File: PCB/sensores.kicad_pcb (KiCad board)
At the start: 2 copper layers, 80.6 x 50 mm, 7 parts, among them P10 CONN_01X07, P11 CONN_01X07, P15 DHT22, P16 GY-87, P2 CONN_01X04, P3 CONN_01X04

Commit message: Add logo ElectronicCats
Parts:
- added G***: LOGO, theinventorhouse:electronic_cats_logo_8x6, F.Cu at (95.5, 94.7)

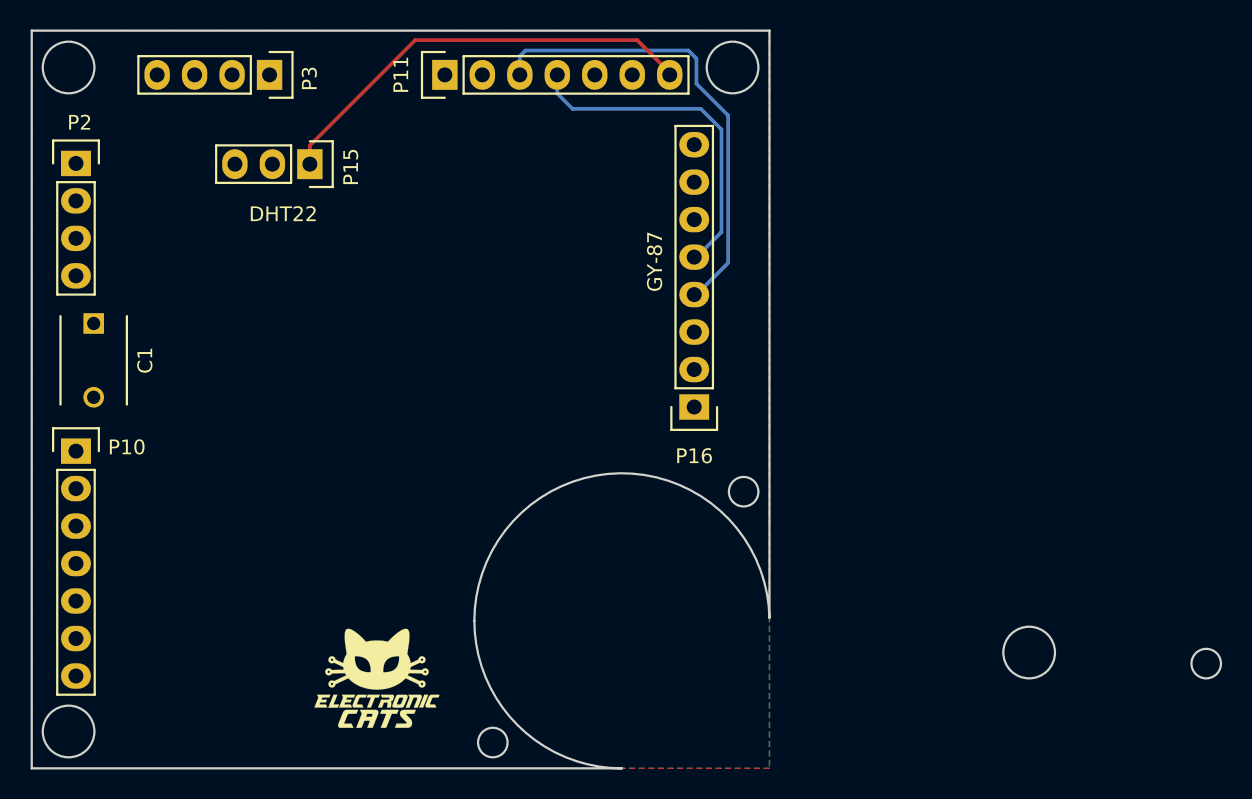
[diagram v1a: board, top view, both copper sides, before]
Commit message: Fix bug GND of GY-87
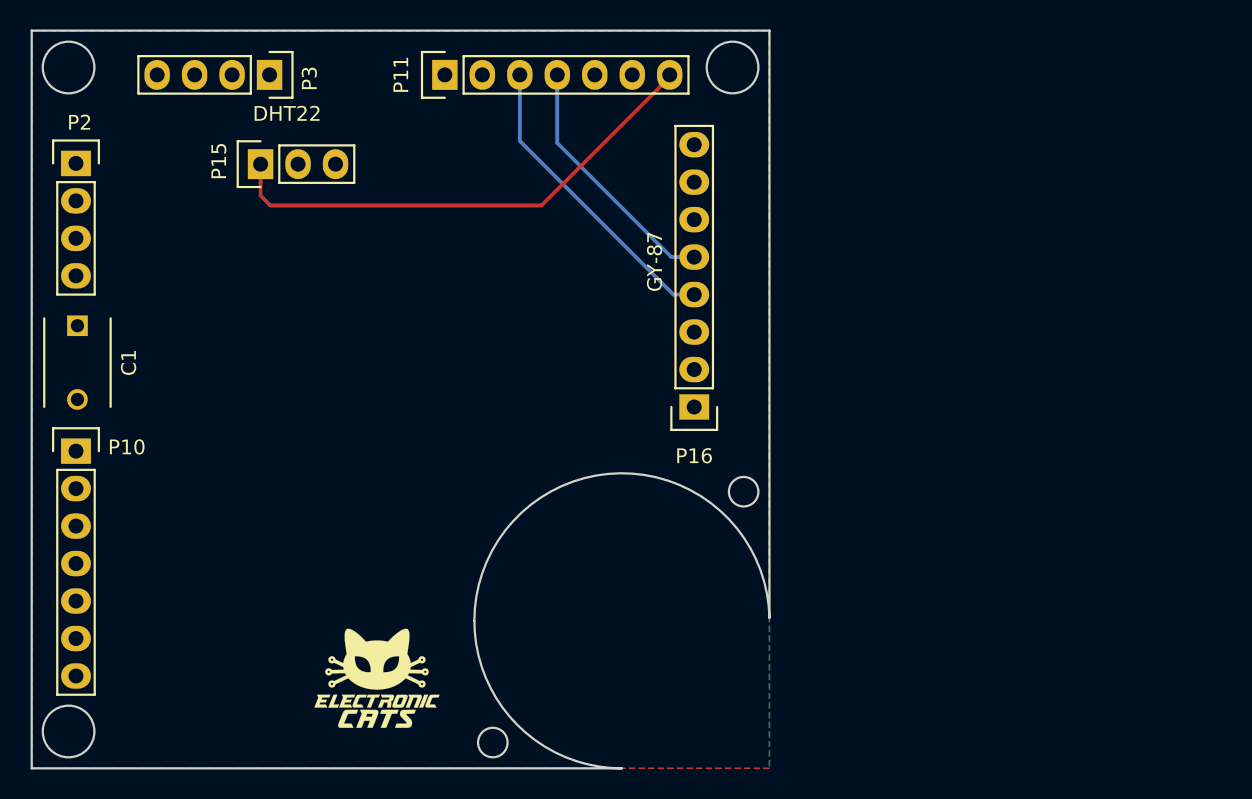
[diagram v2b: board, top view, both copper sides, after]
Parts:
- moved P15 3.34 mm to (87.7, 59.8), turned to 90 degrees
- moved C1 1.11 mm to (75.2, 70.8)
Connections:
- P16 pad 2: GND -> Net-(P16-Pad2)
- P16 pad 3: Net-(P16-Pad3) -> GND
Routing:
- net SCL: track 31.5 -> 20.8 mm
- net SDA: track 22.9 -> 18.5 mm
- net DHT/D6: track 29.7 -> 34.1 mm
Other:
- board size 80.6 x 50 mm -> 50 x 50 mm

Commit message: PCB final
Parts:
- moved P15 1.20 mm to (86.5, 59.8)
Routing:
- net +BATT: track 0.00 -> 78.5 mm
- added copper zone on B.Cu, net GND
- removed copper zone on B.Cu, net +BATT
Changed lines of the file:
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@@
 (kicad_pcb (version 4) (host pcbnew 4.0.0-rc1-stable)
   (general
-    (links 102)
-    (no_connects 72)
-    (area 72.074999 50.674999 122.225001 100.825001)
+    (links 11)
+    (no_connects 4)
+    (area 48.501725 43.9 139.328572 109.450001)
     (thickness 1.6)
     (drawings 22)
-    (tracks 17)
+    (tracks 32)
     (zones 0)
     (modules 8)
@@
     (add_net MOSI)
     (add_net NSS)
-    (add_net "Net-(A1-Pad1)")
-    (add_net "Net-(D1-Pad2)")
-    (add_net "Net-(MODULE1-Pad10)")
-    (add_net "Net-(MODULE1-Pad11)")
-    (add_net "Net-(MODULE1-Pad5)")
-    (add_net "Net-(MODULE1-Pad6)")
-    (add_net "Net-(MODULE1-Pad7)")
-    (add_net "Net-(MODULE1-Pad8)")
     (add_net "Net-(P16-Pad2)")
-    (add_net "Net-(P5-Pad2)")
-    (add_net "Net-(RAW1-Pad1)")
-    (add_net "Net-(RAW1-Pad19)")
-    (add_net "Net-(RAW1-Pad2)")
-    (add_net "Net-(RAW1-Pad21)")
-    (add_net "Net-(RAW1-Pad3)")
-    (add_net "Net-(RAW1-Pad4)")
-    (add_net "Net-(RAW1-Pad5)")
-    (add_net "Net-(RAW1-Pad6)")
-    (add_net "Net-(RAW1-Pad7)")
-    (add_net "Net-(RAW1-Pad8)")
-    (add_net "Net-(RAW1-Pad9)")
-    (add_net "Net-(U1-Pad1)")
-    (add_net "Net-(U1-Pad2)")
-    (add_net "Net-(U2-Pad11)")
-    (add_net "Net-(U2-Pad12)")
-    (add_net "Net-(U2-Pad15)")
-    (add_net "Net-(U2-Pad16)")
-    (add_net "Net-(U2-Pad7)")
     (add_net RST)
     (add_net SCK)
@@
     (add_net S_RX)
     (add_net S_TX)
+  )
+  (module Pin_Headers:Pin_Header_Straight_1x03 (layer F.Cu)
+    (at 86.46 59.8 90)
+    (descr "Through hole pin header")
+    (tags "pin header")
+    (fp_text reference P15 (at 0.2 -2.8 90) (layer F.SilkS)
+      (effects (font (size 1 1) (thickness 0.15)))
+    )
+    (fp_text value DHT22 (at 3.4 1.8 180) (layer F.SilkS)
+      (effects (font (size 1 1) (thickness 0.15)))
+    )
+    (fp_line (start -1.75 -1.75) (end -1.75 6.85) (layer F.CrtYd) (width 0.05))
+    (fp_line (start 1.75 -1.75) (end 1.75 6.85) (layer F.CrtYd) (width 0.05))
+    (fp_line (start -1.75 -1.75) (end 1.75 -1.75) (layer F.CrtYd) (width 0.05))
+    (fp_line (start -1.75 6.85) (end 1.75 6.85) (layer F.CrtYd) (width 0.05))
+    (fp_line (start -1.27 1.27) (end -1.27 6.35) (layer F.SilkS) (width 0.15))
+    (fp_line (start -1.27 6.35) (end 1.27 6.35) (layer F.SilkS) (width 0.15))
+    (fp_line (start 1.27 6.35) (end 1.27 1.27) (layer F.SilkS) (width 0.15))
+    (fp_line (start 1.55 -1.55) (end 1.55 0) (layer F.SilkS) (width 0.15))
+    (fp_line (start 1.27 1.27) (end -1.27 1.27) (layer F.SilkS) (width 0.15))
+    (fp_line (start -1.55 0) (end -1.55 -1.55) (layer F.SilkS) (width 0.15))
+    (fp_line (start -1.55 -1.55) (end 1.55 -1.55) (layer F.SilkS) (width 0.15))
+    (pad 1 thru_hole rect (at 0 0 90) (size 2.032 1.7272) (drill 1.016) (layers *.Cu *.Mask F.SilkS)
+      (net 7 DHT/D6))
+    (pad 2 thru_hole oval (at 0 2.54 90) (size 2.032 1.7272) (drill 1.016) (layers *.Cu *.Mask F.SilkS)
+      (net 2 +BATT))
+    (pad 3 thru_hole oval (at 0 5.08 90) (size 2.032 1.7272) (drill 1.016) (layers *.Cu *.Mask F.SilkS)
+      (net 1 GND))
+    (model Pin_Headers.3dshapes/Pin_Header_Straight_1x03.wrl
+      (at (xyz 0 -0.1 0))
+      (scale (xyz 1 1 1))
+      (rotate (xyz 0 0 90))
+    )
   )
   (module Pin_Headers:Pin_Header_Straight_1x08 (layer F.Cu)
@@
     (model Pin_Headers.3dshapes/Pin_Header_Straight_1x07.wrl
       (at (xyz 0 -0.3 0))
-      (scale (xyz 1 1 1))
-      (rotate (xyz 0 0 90))
-    )
-  )
-  (module Pin_Headers:Pin_Header_Straight_1x03 (layer F.Cu)
-    (at 87.66 59.8 90)
-    (descr "Through hole pin header")
-    (tags "pin header")
-    (fp_text reference P15 (at 0.2 -2.8 90) (layer F.SilkS)
-      (effects (font (size 1 1) (thickness 0.15)))
-    )
-    (fp_text value DHT22 (at 3.4 1.8 180) (layer F.SilkS)
-      (effects (font (size 1 1) (thickness 0.15)))
-    )
-    (fp_line (start -1.75 -1.75) (end -1.75 6.85) (layer F.CrtYd) (width 0.05))
-    (fp_line (start 1.75 -1.75) (end 1.75 6.85) (layer F.CrtYd) (width 0.05))
-    (fp_line (start -1.75 -1.75) (end 1.75 -1.75) (layer F.CrtYd) (width 0.05))
-    (fp_line (start -1.75 6.85) (end 1.75 6.85) (layer F.CrtYd) (width 0.05))
-    (fp_line (start -1.27 1.27) (end -1.27 6.35) (layer F.SilkS) (width 0.15))
-    (fp_line (start -1.27 6.35) (end 1.27 6.35) (layer F.SilkS) (width 0.15))
-    (fp_line (start 1.27 6.35) (end 1.27 1.27) (layer F.SilkS) (width 0.15))
-    (fp_line (start 1.55 -1.55) (end 1.55 0) (layer F.SilkS) (width 0.15))
-    (fp_line (start 1.27 1.27) (end -1.27 1.27) (layer F.SilkS) (width 0.15))
-    (fp_line (start -1.55 0) (end -1.55 -1.55) (layer F.SilkS) (width 0.15))
-    (fp_line (start -1.55 -1.55) (end 1.55 -1.55) (layer F.SilkS) (width 0.15))
-    (pad 1 thru_hole rect (at 0 0 90) (size 2.032 1.7272) (drill 1.016) (layers *.Cu *.Mask F.SilkS)
-      (net 7 DHT/D6))
-    (pad 2 thru_hole oval (at 0 2.54 90) (size 2.032 1.7272) (drill 1.016) (layers *.Cu *.Mask F.SilkS)
-      (net 2 +BATT))
-    (pad 3 thru_hole oval (at 0 5.08 90) (size 2.032 1.7272) (drill 1.016) (layers *.Cu *.Mask F.SilkS)
-      (net 1 GND))
-    (model Pin_Headers.3dshapes/Pin_Header_Straight_1x03.wrl
-      (at (xyz 0 -0.1 0))
       (scale (xyz 1 1 1))
       (rotate (xyz 0 0 90))
@@
   (gr_line (start 72.15 100.75) (end 72.15 50.75) (layer Edge.Cuts) (width 0.15))
   (gr_line (start 72.15 50.75) (end 122.15 50.75) (layer Edge.Cuts) (width 0.15))
+  (segment (start 89 59.8) (end 89 61.066) (width 0.25) (layer B.Cu) (net 2))
+  (segment (start 89 61.066) (end 90.2 62.266) (width 0.25) (layer B.Cu) (net 2))
+  (segment (start 90.2 62.266) (end 90.2 65.8) (width 0.25) (layer B.Cu) (net 2))
+  (segment (start 75.15 79.25) (end 76.75 79.25) (width 0.25) (layer B.Cu) (net 2) (status 400000))
+  (segment (start 77.4 72.9) (end 75.25 70.75) (width 0.25) (layer B.Cu) (net 2) (status 800000))
+  (segment (start 77.4 78.6) (end 77.4 72.9) (width 0.25) (layer B.Cu) (net 2))
+  (segment (start 76.75 79.25) (end 77.4 78.6) (width 0.25) (layer B.Cu) (net 2))
+  (segment (start 101.8 65.8) (end 102.69 65.8) (width 0.25) (layer B.Cu) (net 2))
+  (segment (start 102.69 53.75) (end 102.69 65.8) (width 0.25) (layer B.Cu) (net 2) (status 400000))
+  (segment (start 102.69 65.8) (end 102.69 66.69) (width 0.25) (layer B.Cu) (net 2))
+  (segment (start 102.69 66.69) (end 102.8 66.8) (width 0.25) (layer B.Cu) (net 2))
+  (segment (start 90.2 65.8) (end 101.8 65.8) (width 0.25) (layer B.Cu) (net 2))
+  (segment (start 112.26 76.26) (end 117.05 76.26) (width 0.25) (layer B.Cu) (net 2) (status 800000))
+  (segment (start 102.8 66.8) (end 112.26 76.26) (width 0.25) (layer B.Cu) (net 2))
+  (segment (start 75.25 70.75) (end 85.25 70.75) (width 0.25) (layer B.Cu) (net 2) (status 400000))
+  (segment (start 85.25 70.75) (end 90.2 65.8) (width 0.25) (layer B.Cu) (net 2))
   (segment (start 105.23 58.23) (end 115.64 68.64) (width 0.25) (layer B.Cu) (net 5))
   (segment (start 115.64 68.64) (end 117.05 68.64) (width 0.25) (layer B.Cu) (net 5))
@@
   (segment (start 117.2024 66.1) (end 117.05 66.1) (width 0.25) (layer B.Cu) (net 6))
   (segment (start 107.77 53.75) (end 107.77 55.016) (width 0.25) (layer B.Cu) (net 6))
-  (segment (start 87.66 61.066) (end 87.66 61.94) (width 0.25) (layer F.Cu) (net 7))
-  (segment (start 87.66 61.94) (end 88.32 62.6) (width 0.25) (layer F.Cu) (net 7))
-  (segment (start 88.32 62.6) (end 106.6924 62.6) (width 0.25) (layer F.Cu) (net 7))
+  (segment (start 89.1076 62.6) (end 86.46 59.9524) (width 0.25) (layer F.Cu) (net 7))
+  (segment (start 86.46 59.9524) (end 86.46 59.8) (width 0.25) (layer F.Cu) (net 7))
+  (segment (start 106.6924 62.6) (end 89.1076 62.6) (width 0.25) (layer F.Cu) (net 7))
   (segment (start 106.6924 62.6) (end 115.39 53.9024) (width 0.25) (layer F.Cu) (net 7))
   (segment (start 115.39 53.9024) (end 115.39 53.75) (width 0.25) (layer F.Cu) (net 7))
-  (segment (start 87.66 59.8) (end 87.66 61.066) (width 0.25) (layer F.Cu) (net 7))
   (segment (start 115.39 53.5976) (end 115.39 53.75) (width 0.25) (layer F.Cu) (net 7))
   (segment (start 116.8976 73.72) (end 117.05 73.72) (width 0.25) (layer F.Cu) (net 24))
-  (zone (net 2) (net_name +BATT) (layer B.Cu) (hatch edge 0.508)
-    (connect_pads (clearance 0.8))
-    (min_thickness 0.254)
-    (fill yes (arc_segments 16) (thermal_gap 0.508) (thermal_bridge_width 0.508))
-    (polygon
-      (pts
-        (xy 72.15 50.75) (xy 122.15 50.75) (xy 122.15 100.75) (xy 72.15 100.75)
-      )
-    )
-  )
   (zone (net 1) (net_name GND) (layer F.Cu) (hatch edge 0.508)
     (connect_pads (clearance 0.8))
@@
     (polygon
       (pts
-        (xy 72.15 50.75) (xy 122.15 50.75) (xy 122.15 100.75) (xy 72.15 100.75)
+        (xy 72.2 50.8) (xy 122.2 50.8) (xy 122.4 100.8) (xy 72 100.8)
       )
     )
+  )
+  (zone (net 1) (net_name GND) (layer B.Cu) (hatch edge 0.508)
+    (connect_pads (clearance 0.8))
+    (min_thickness 0.254)
+    (fill yes (arc_segments 16) (thermal_gap 0.508) (thermal_bridge_width 0.508))
+    (polygon
+      (pts
+        (xy 72.2 50.8) (xy 122.2 50.8) (xy 122.4 100.8) (xy 72.2 100.6)
+      )
+    )

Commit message: Fix details
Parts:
- added REF**: Symbol_OSHW-Logo_SilkScreen_BIG, Symbols:Symbol_OSHW-Logo_SilkScreen_BIG, B.Cu at (92.4, 52.6)
- G***: moved to B.Cu
- moved G*** 7.88 mm to (88.0, 92.4), turned to 180 degrees
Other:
- board text added: "Sensor Board"
